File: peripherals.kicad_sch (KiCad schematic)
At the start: 21 parts, among them J10 Cam 3, J11 Servo, J12 Cam 2, J2 Encoder, J9 Cam 1, Q1 BSS816NWH6327XTSA1, Q2 NPN, Q3 BSS816NWH6327XTSA1, Q6 BSS816NWH6327XTSA1

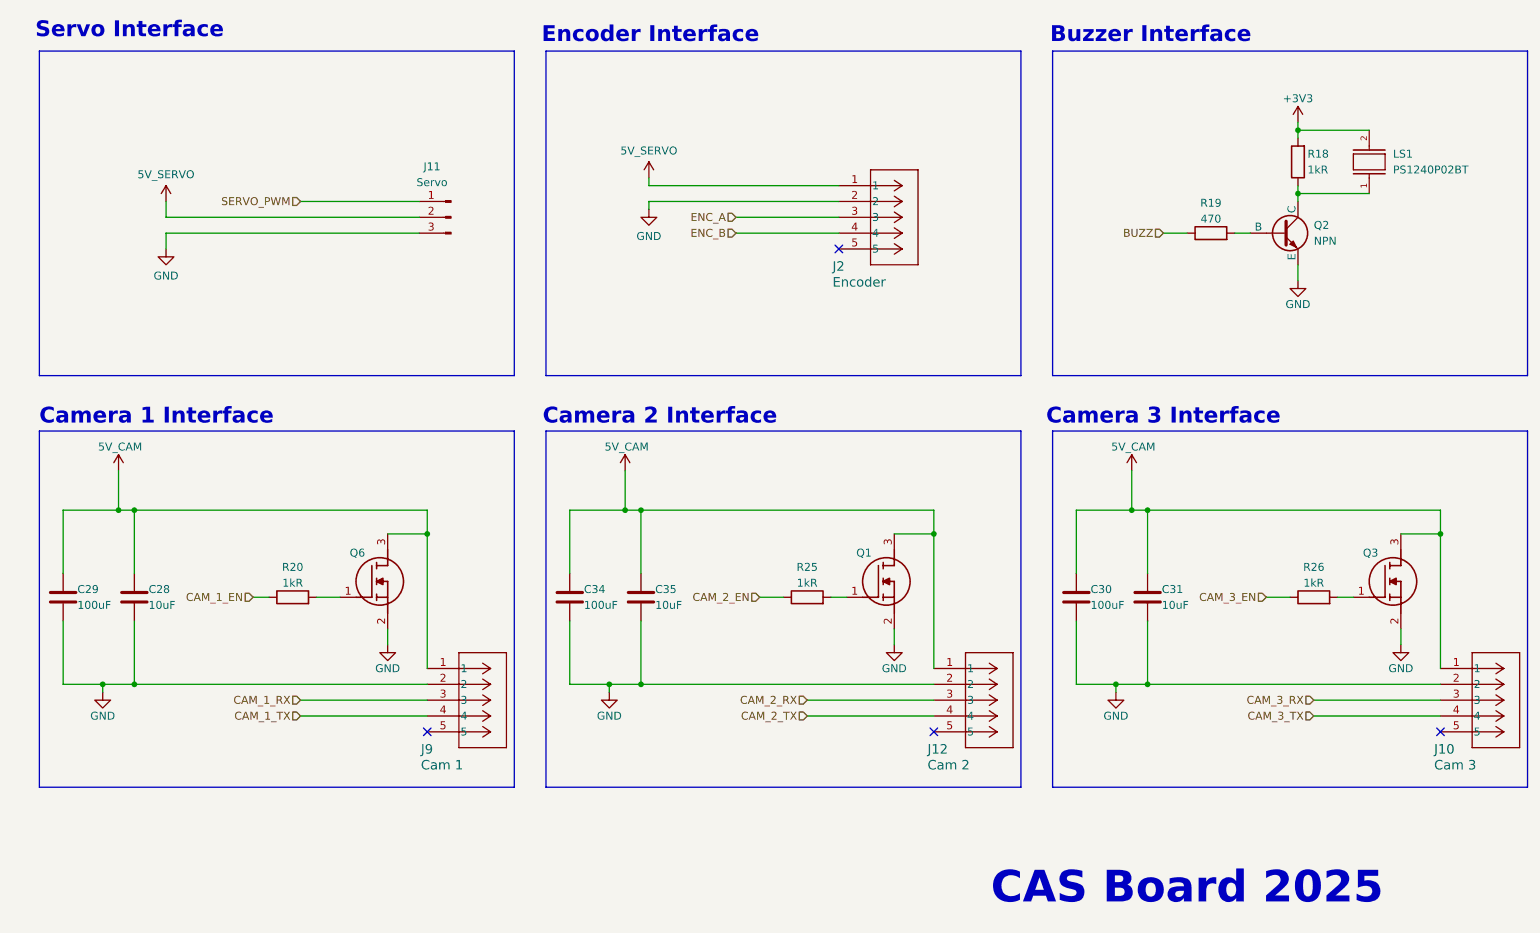
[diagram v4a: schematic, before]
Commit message: Initial layout for PCB components, updated README with images. Removed some test points and headers from final layout. Pending addition of buzzer. Pending additional power testing and pending routing.
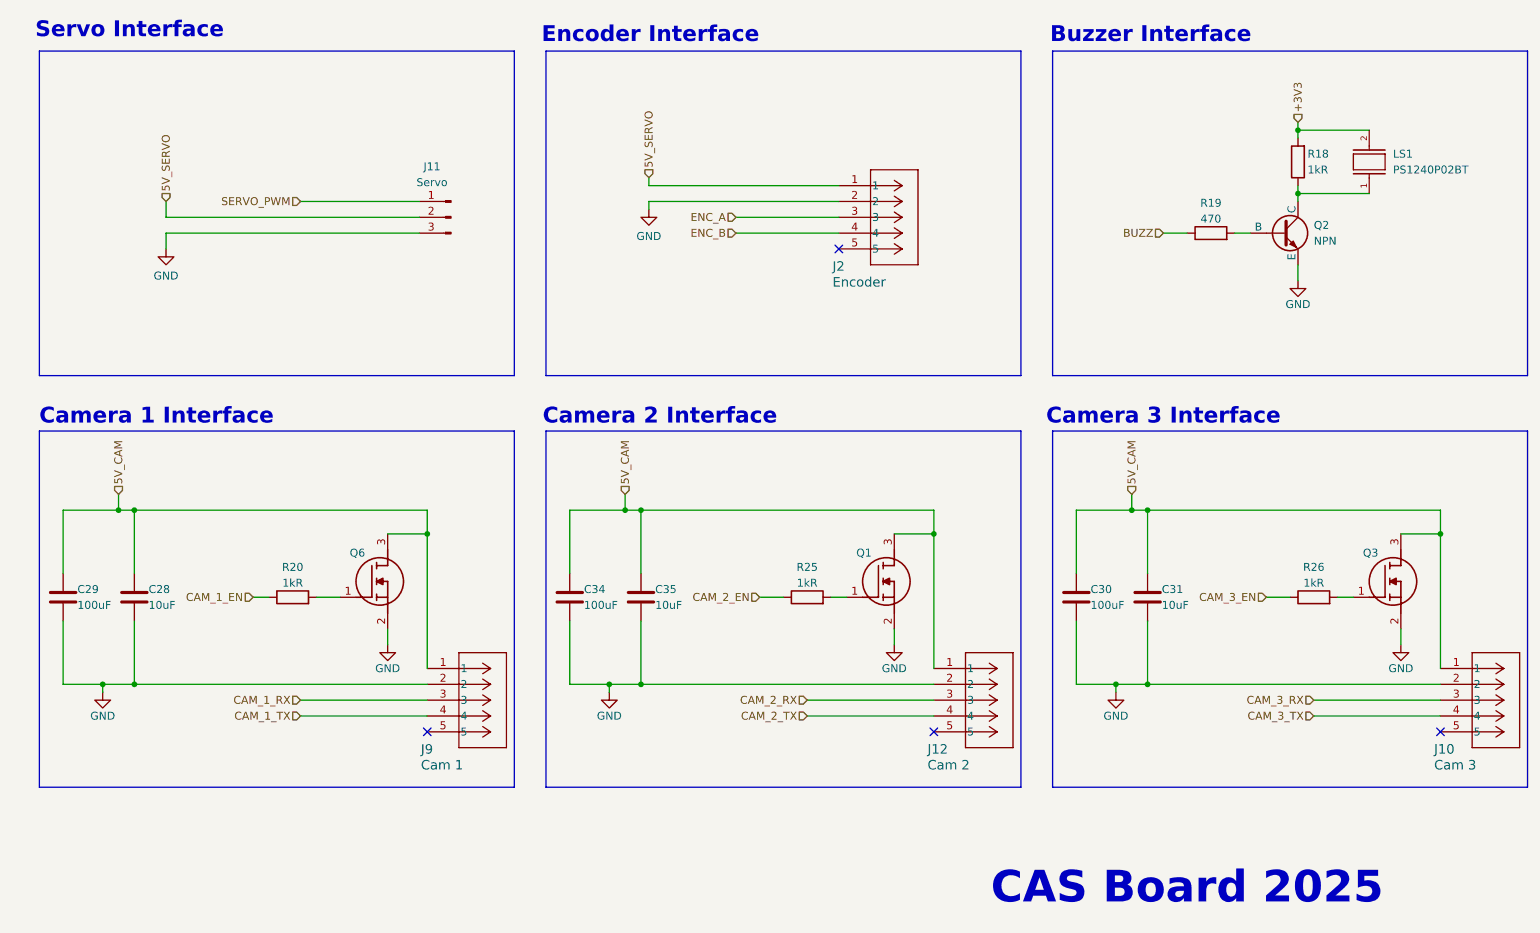
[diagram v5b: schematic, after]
